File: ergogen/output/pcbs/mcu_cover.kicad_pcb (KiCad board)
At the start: 2 copper layers, 20.5 x 58 mm, 2 parts

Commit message: new shape
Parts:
- moved MH1 3.63 mm to (149.5, 86.4)
- moved MH2 2.39 mm to (163.5, 94.5)
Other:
- board size 20.5 x 58 mm -> 20.2 x 59 mm
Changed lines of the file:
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@@
   (title_block
     (title "mcu_cover")
-    (date "2025-11-02")
+    (date "2025-11-10")
     (rev "1")
     (company "curtis bollinger")
@@
   (footprint "ceoloide:mounting_hole_npth"
     (layer "F.Cu")
-    (at 151.2922031 89.53066630000001 0)
+    (at 149.48162050000002 86.38459739999999 0)
     (property "Reference" "MH1"
       (at 0 2.55 0)
@@
   (footprint "ceoloide:mounting_hole_npth"
     (layer "F.Cu")
-    (at 165.2922031 96.03066630000001 0)
+    (at 163.48162050000002 94.46459739999999 0)
     (property "Reference" "MH2"
       (at 0 2.55 0)
@@
     )
   )
-  (gr_line (start 168.7922031 100.07308144572157) (end 168.7922031 44.03066630000001) (layer Edge.Cuts) (stroke (width 0.15) (type default)))
-(gr_line (start 167.7922031 43.03066630000001) (end 149.2922031 43.03066630000001) (layer Edge.Cuts) (stroke (width 0.15) (type default)))
-(gr_line (start 148.2922031 90.64686063325334) (end 148.2922031 44.03066630000001) (layer Edge.Cuts) (stroke (width 0.15) (type default)))
-(gr_line (start 148.8382126 91.53786713325334) (end 167.33821260000002 100.96408794572159) (layer Edge.Cuts) (stroke (width 0.15) (type default)))
-(gr_line (start 153.1922031 76.93066630000001) (end 162.9922031 76.93066630000001) (layer Edge.Cuts) (stroke (width 0.15) (type default)))
-(gr_line (start 163.4922031 76.43066630000001) (end 163.4922031 52.130666300000016) (layer Edge.Cuts) (stroke (width 0.15) (type default)))
-(gr_line (start 162.9922031 51.630666300000016) (end 153.1922031 51.630666300000016) (layer Edge.Cuts) (stroke (width 0.15) (type default)))
-(gr_line (start 152.6922031 52.130666300000016) (end 152.6922031 76.43066630000001) (layer Edge.Cuts) (stroke (width 0.15) (type default)))
-(gr_arc (start 162.9922031 76.93066630000001) (mid 163.34575650000002 76.78421970000001) (end 163.4922031 76.43066630000001) (layer Edge.Cuts) (stroke (width 0.15) (type default)))
-(gr_arc (start 163.4922031 52.130666300000016) (mid 163.34575650000002 51.77711290000001) (end 162.9922031 51.630666300000016) (layer Edge.Cuts) (stroke (width 0.15) (type default)))
-(gr_arc (start 153.1922031 51.630666300000016) (mid 152.8386497 51.77711290000001) (end 152.6922031 52.130666300000016) (layer Edge.Cuts) (stroke (width 0.15) (type default)))
-(gr_arc (start 152.6922031 76.43066630000001) (mid 152.8386497 76.78421970000001) (end 153.1922031 76.93066630000001) (layer Edge.Cuts) (stroke (width 0.15) (type default)))
-(gr_arc (start 168.7922031 44.03066630000001) (mid 168.4993099 43.32355950000001) (end 167.7922031 43.03066630000001) (layer Edge.Cuts) (stroke (width 0.15) (type default)))
-(gr_arc (start 149.2922031 43.03066630000001) (mid 148.5850963 43.32355950000001) (end 148.2922031 44.03066630000001) (layer Edge.Cuts) (stroke (width 0.15) (type default)))
-(gr_arc (start 148.2922031 90.64686063325334) (mid 148.4395629 91.16935923325335) (end 148.8382126 91.53786713325334) (layer Edge.Cuts) (stroke (width 0.15) (type default)))
-(gr_arc (start 167.3382126 100.96408794572157) (mid 168.3147016 100.92572154572157) (end 168.7922031 100.07308144572157) (layer Edge.Cuts) (stroke (width 0.15) (type default)))
-(gr_circle (center 151.2922031 89.53066630000001) (end 152.2922031 89.53066630000001) (layer Edge.Cuts) (stroke (width 0.15) (type default)) (fill none))
-(gr_circle (center 165.2922031 96.03066630000001) (end 166.2922031 96.03066630000001) (layer Edge.Cuts) (stroke (width 0.15) (type default)) (fill none))
+  (gr_line (start 166.73162050017376 96.47131793428673) (end 166.73162050017376 41.4845974) (layer Edge.Cuts) (stroke (width 0.15) (type default)))
+(gr_line (start 164.73162050017376 39.4845974) (end 148.55712050000002 39.4845974) (layer Edge.Cuts) (stroke (width 0.15) (type default)))
+(gr_line (start 146.55712050000002 85.97848666737389) (end 146.55712050000002 41.4845974) (layer Edge.Cuts) (stroke (width 0.15) (type default)))
+(gr_line (start 148.55712050000005 89.44258826737392) (end 157.02419341559587 94.33105510345534) (layer Edge.Cuts) (stroke (width 0.15) (type default)))
+(gr_arc (start 146.55712050000002 85.97848666737389) (mid 147.09301890000003 87.97848666737389) (end 148.55712050000002 89.44258826737389) (layer Edge.Cuts) (stroke (width 0.15) (type default)))
+(gr_line (start 163.73162050017373 98.20336873428671) (end 157.0242892 94.33088919999997) (layer Edge.Cuts) (stroke (width 0.15) (type default)))
+(gr_line (start 157.0242892 94.33088919999997) (end 157.02419341559587 94.33105510345536) (layer Edge.Cuts) (stroke (width 0.15) (type default)))
+(gr_line (start 151.38162050000003 73.7845974) (end 161.18162050000004 73.7845974) (layer Edge.Cuts) (stroke (width 0.15) (type default)))
+(gr_line (start 161.68162050000004 73.2845974) (end 161.68162050000004 48.9845974) (layer Edge.Cuts) (stroke (width 0.15) (type default)))
+(gr_line (start 161.18162050000004 48.4845974) (end 151.38162050000003 48.4845974) (layer Edge.Cuts) (stroke (width 0.15) (type default)))
+(gr_line (start 150.88162050000003 48.9845974) (end 150.88162050000003 73.2845974) (layer Edge.Cuts) (stroke (width 0.15) (type default)))
+(gr_arc (start 161.18162050000004 73.7845974) (mid 161.53517390000005 73.63815079999999) (end 161.68162050000004 73.2845974) (layer Edge.Cuts) (stroke (width 0.15) (type default)))
+(gr_arc (start 161.68162050000004 48.9845974) (mid 161.53517390000005 48.631043999999996) (end 161.18162050000004 48.4845974) (layer Edge.Cuts) (stroke (width 0.15) (type default)))
+(gr_arc (start 151.38162050000003 48.4845974) (mid 151.02806710000002 48.631043999999996) (end 150.88162050000003 48.9845974) (layer Edge.Cuts) (stroke (width 0.15) (type default)))
+(gr_arc (start 150.88162050000003 73.2845974) (mid 151.02806710000002 73.63815079999999) (end 151.38162050000003 73.7845974) (layer Edge.Cuts) (stroke (width 0.15) (type default)))
+(gr_arc (start 166.73162050017376 41.4845974) (mid 166.14583410017377 40.0703838) (end 164.73162050017376 39.4845974) (layer Edge.Cuts) (stroke (width 0.15) (type default)))
+(gr_arc (start 148.55712050000002 39.4845974) (mid 147.1429069 40.0703838) (end 146.55712050000002 41.4845974) (layer Edge.Cuts) (stroke (width 0.15) (type default)))
+(gr_arc (start 163.73162050017376 98.20336873428673) (mid 165.73162050017376 98.20336873428673) (end 166.73162050017376 96.47131793428673) (layer Edge.Cuts) (stroke (width 0.15) (type default)))
+(gr_circle (center 149.48162050000002 86.38459739999999) (end 150.48162050000002 86.38459739999999) (layer Edge.Cuts) (stroke (width 0.15) (type default)) (fill none))
+(gr_circle (center 163.48162050000002 94.46459739999999) (end 164.48162050000002 94.46459739999999) (layer Edge.Cuts) (stroke (width 0.15) (type default)) (fill none))
 )

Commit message: update generated files
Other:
- board size 20.2 x 59 mm -> 20.2 x 59.7 mm
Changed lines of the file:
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@@
   (title_block
     (title "mcu_cover")
-    (date "2025-11-10")
+    (date "2025-11-12")
     (rev "1")
     (company "curtis bollinger")
@@
     )
   )
-  (gr_line (start 166.73162050017376 96.47131793428673) (end 166.73162050017376 41.4845974) (layer Edge.Cuts) (stroke (width 0.15) (type default)))
-(gr_line (start 164.73162050017376 39.4845974) (end 148.55712050000002 39.4845974) (layer Edge.Cuts) (stroke (width 0.15) (type default)))
-(gr_line (start 146.55712050000002 85.97848666737389) (end 146.55712050000002 41.4845974) (layer Edge.Cuts) (stroke (width 0.15) (type default)))
+  (gr_line (start 166.73162050017376 98.20336873864981) (end 166.73162050000002 43.4845974) (layer Edge.Cuts) (stroke (width 0.15) (type default)))
+(gr_line (start 147.55712050000002 39.4845974) (end 162.73162050000002 39.4845974) (layer Edge.Cuts) (stroke (width 0.15) (type default)))
+(gr_arc (start 166.73162050000002 43.4845974) (mid 165.56004760000002 40.6561703) (end 162.73162050000002 39.4845974) (layer Edge.Cuts) (stroke (width 0.15) (type default)))
+(gr_line (start 146.55712050000002 85.97848666737389) (end 146.55712050000002 40.4845974) (layer Edge.Cuts) (stroke (width 0.15) (type default)))
 (gr_line (start 148.55712050000005 89.44258826737392) (end 157.02419341559587 94.33105510345534) (layer Edge.Cuts) (stroke (width 0.15) (type default)))
 (gr_arc (start 146.55712050000002 85.97848666737389) (mid 147.09301890000003 87.97848666737389) (end 148.55712050000002 89.44258826737389) (layer Edge.Cuts) (stroke (width 0.15) (type default)))
-(gr_line (start 163.73162050017373 98.20336873428671) (end 157.0242892 94.33088919999997) (layer Edge.Cuts) (stroke (width 0.15) (type default)))
+(gr_line (start 165.23162050017376 99.06939413864981) (end 157.0242892 94.33088919999997) (layer Edge.Cuts) (stroke (width 0.15) (type default)))
 (gr_line (start 157.0242892 94.33088919999997) (end 157.02419341559587 94.33105510345536) (layer Edge.Cuts) (stroke (width 0.15) (type default)))
 (gr_line (start 151.38162050000003 73.7845974) (end 161.18162050000004 73.7845974) (layer Edge.Cuts) (stroke (width 0.15) (type default)))
@@
 (gr_arc (start 151.38162050000003 48.4845974) (mid 151.02806710000002 48.631043999999996) (end 150.88162050000003 48.9845974) (layer Edge.Cuts) (stroke (width 0.15) (type default)))
 (gr_arc (start 150.88162050000003 73.2845974) (mid 151.02806710000002 73.63815079999999) (end 151.38162050000003 73.7845974) (layer Edge.Cuts) (stroke (width 0.15) (type default)))
-(gr_arc (start 166.73162050017376 41.4845974) (mid 166.14583410017377 40.0703838) (end 164.73162050017376 39.4845974) (layer Edge.Cuts) (stroke (width 0.15) (type default)))
-(gr_arc (start 148.55712050000002 39.4845974) (mid 147.1429069 40.0703838) (end 146.55712050000002 41.4845974) (layer Edge.Cuts) (stroke (width 0.15) (type default)))
-(gr_arc (start 163.73162050017376 98.20336873428673) (mid 165.73162050017376 98.20336873428673) (end 166.73162050017376 96.47131793428673) (layer Edge.Cuts) (stroke (width 0.15) (type default)))
+(gr_arc (start 147.55712050000002 39.4845974) (mid 146.85001370000003 39.7774906) (end 146.55712050000002 40.4845974) (layer Edge.Cuts) (stroke (width 0.15) (type default)))
+(gr_arc (start 165.23162050017376 99.06939413864981) (mid 166.23162050017376 99.06939413864981) (end 166.73162050017376 98.20336873864981) (layer Edge.Cuts) (stroke (width 0.15) (type default)))
 (gr_circle (center 149.48162050000002 86.38459739999999) (end 150.48162050000002 86.38459739999999) (layer Edge.Cuts) (stroke (width 0.15) (type default)) (fill none))
 (gr_circle (center 163.48162050000002 94.46459739999999) (end 164.48162050000002 94.46459739999999) (layer Edge.Cuts) (stroke (width 0.15) (type default)) (fill none))

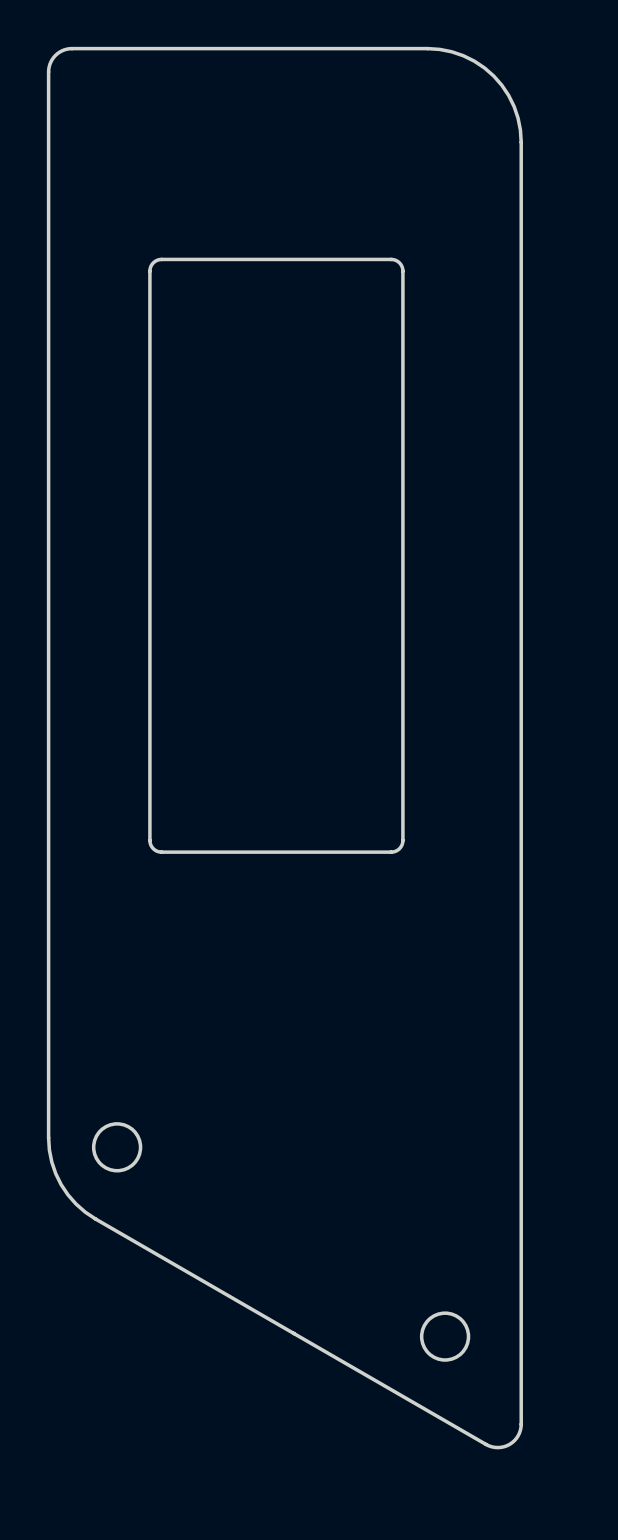
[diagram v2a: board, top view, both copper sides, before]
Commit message: working on new case
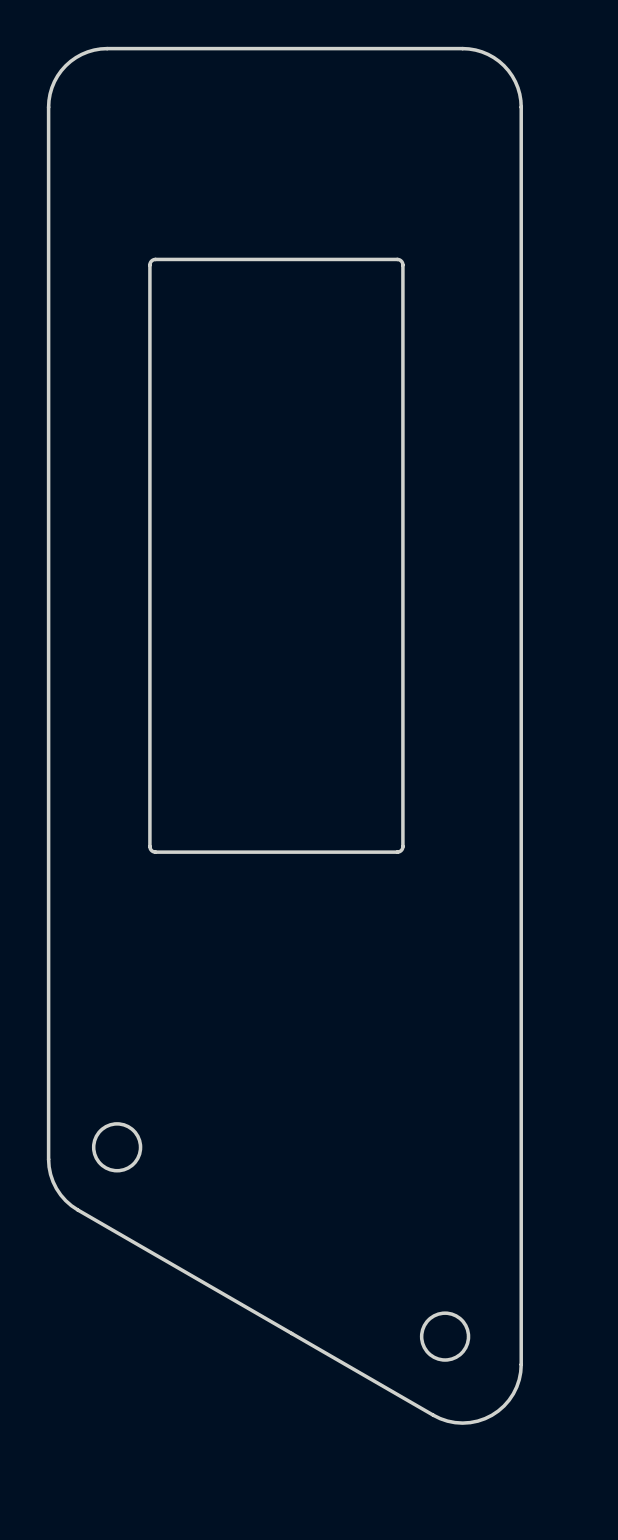
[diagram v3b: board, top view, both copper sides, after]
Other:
- board size 20.2 x 59.7 mm -> 20.2 x 58.7 mm
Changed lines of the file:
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@@
     )
   )
-  (gr_line (start 166.73162050017376 98.20336873864981) (end 166.73162050000002 43.4845974) (layer Edge.Cuts) (stroke (width 0.15) (type default)))
-(gr_line (start 147.55712050000002 39.4845974) (end 162.73162050000002 39.4845974) (layer Edge.Cuts) (stroke (width 0.15) (type default)))
-(gr_arc (start 166.73162050000002 43.4845974) (mid 165.56004760000002 40.6561703) (end 162.73162050000002 39.4845974) (layer Edge.Cuts) (stroke (width 0.15) (type default)))
-(gr_line (start 146.55712050000002 85.97848666737389) (end 146.55712050000002 40.4845974) (layer Edge.Cuts) (stroke (width 0.15) (type default)))
-(gr_line (start 148.55712050000005 89.44258826737392) (end 157.02419341559587 94.33105510345534) (layer Edge.Cuts) (stroke (width 0.15) (type default)))
-(gr_arc (start 146.55712050000002 85.97848666737389) (mid 147.09301890000003 87.97848666737389) (end 148.55712050000002 89.44258826737389) (layer Edge.Cuts) (stroke (width 0.15) (type default)))
-(gr_line (start 165.23162050017376 99.06939413864981) (end 157.0242892 94.33088919999997) (layer Edge.Cuts) (stroke (width 0.15) (type default)))
-(gr_line (start 157.0242892 94.33088919999997) (end 157.02419341559587 94.33105510345536) (layer Edge.Cuts) (stroke (width 0.15) (type default)))
-(gr_line (start 151.38162050000003 73.7845974) (end 161.18162050000004 73.7845974) (layer Edge.Cuts) (stroke (width 0.15) (type default)))
-(gr_line (start 161.68162050000004 73.2845974) (end 161.68162050000004 48.9845974) (layer Edge.Cuts) (stroke (width 0.15) (type default)))
-(gr_line (start 161.18162050000004 48.4845974) (end 151.38162050000003 48.4845974) (layer Edge.Cuts) (stroke (width 0.15) (type default)))
-(gr_line (start 150.88162050000003 48.9845974) (end 150.88162050000003 73.2845974) (layer Edge.Cuts) (stroke (width 0.15) (type default)))
-(gr_arc (start 161.18162050000004 73.7845974) (mid 161.53517390000005 73.63815079999999) (end 161.68162050000004 73.2845974) (layer Edge.Cuts) (stroke (width 0.15) (type default)))
-(gr_arc (start 161.68162050000004 48.9845974) (mid 161.53517390000005 48.631043999999996) (end 161.18162050000004 48.4845974) (layer Edge.Cuts) (stroke (width 0.15) (type default)))
-(gr_arc (start 151.38162050000003 48.4845974) (mid 151.02806710000002 48.631043999999996) (end 150.88162050000003 48.9845974) (layer Edge.Cuts) (stroke (width 0.15) (type default)))
-(gr_arc (start 150.88162050000003 73.2845974) (mid 151.02806710000002 73.63815079999999) (end 151.38162050000003 73.7845974) (layer Edge.Cuts) (stroke (width 0.15) (type default)))
-(gr_arc (start 147.55712050000002 39.4845974) (mid 146.85001370000003 39.7774906) (end 146.55712050000002 40.4845974) (layer Edge.Cuts) (stroke (width 0.15) (type default)))
-(gr_arc (start 165.23162050017376 99.06939413864981) (mid 166.23162050017376 99.06939413864981) (end 166.73162050017376 98.20336873864981) (layer Edge.Cuts) (stroke (width 0.15) (type default)))
+  (gr_line (start 166.7316204652048 95.6574636595821) (end 166.7316204652048 41.9845974) (layer Edge.Cuts) (stroke (width 0.15) (type default)))
+(gr_line (start 164.2316204652048 39.4845974) (end 149.05712050000002 39.4845974) (layer Edge.Cuts) (stroke (width 0.15) (type default)))
+(gr_line (start 146.55712050000002 86.89647358900609) (end 146.55712050000002 41.9845974) (layer Edge.Cuts) (stroke (width 0.15) (type default)))
+(gr_line (start 147.8071205 89.06153708900608) (end 156.9341933851923 94.33105508590181) (layer Edge.Cuts) (stroke (width 0.15) (type default)))
+(gr_arc (start 146.55712050000002 86.89647358900609) (mid 146.89205700000002 88.14647358900609) (end 147.80712050000002 89.0615370890061) (layer Edge.Cuts) (stroke (width 0.15) (type default)))
+(gr_line (start 162.98162046347275 97.82252715858212) (end 156.9341984 94.33104639999999) (layer Edge.Cuts) (stroke (width 0.15) (type default)))
+(gr_arc (start 166.7316204652048 41.9845974) (mid 165.9993874652048 40.2168304) (end 164.2316204652048 39.4845974) (layer Edge.Cuts) (stroke (width 0.15) (type default)))
+(gr_arc (start 149.05712050000002 39.4845974) (mid 147.28935350000003 40.2168304) (end 146.55712050000002 41.9845974) (layer Edge.Cuts) (stroke (width 0.15) (type default)))
+(gr_arc (start 162.9816204652048 97.82252715958211) (mid 165.4816204652048 97.82252715958211) (end 166.7316204652048 95.6574636595821) (layer Edge.Cuts) (stroke (width 0.15) (type default)))
+(gr_line (start 151.12162050000003 73.7845974) (end 161.44162050000003 73.7845974) (layer Edge.Cuts) (stroke (width 0.15) (type default)))
+(gr_line (start 161.68162050000004 73.5445974) (end 161.68162050000004 48.7245974) (layer Edge.Cuts) (stroke (width 0.15) (type default)))
+(gr_line (start 161.44162050000003 48.4845974) (end 151.12162050000003 48.4845974) (layer Edge.Cuts) (stroke (width 0.15) (type default)))
+(gr_line (start 150.88162050000003 48.7245974) (end 150.88162050000003 73.5445974) (layer Edge.Cuts) (stroke (width 0.15) (type default)))
+(gr_arc (start 162.9816204652048 97.82252715958211) (mid 162.9816204652048 97.82252715958211) (end 162.9816204652048 97.82252715958211) (layer Edge.Cuts) (stroke (width 0.15) (type default)))
+(gr_arc (start 161.44162050000003 73.7845974) (mid 161.6113261 73.714303) (end 161.68162050000004 73.5445974) (layer Edge.Cuts) (stroke (width 0.15) (type default)))
+(gr_arc (start 161.68162050000004 48.7245974) (mid 161.6113261 48.5548918) (end 161.44162050000003 48.4845974) (layer Edge.Cuts) (stroke (width 0.15) (type default)))
+(gr_arc (start 151.12162050000003 48.4845974) (mid 150.95191490000005 48.5548918) (end 150.88162050000003 48.7245974) (layer Edge.Cuts) (stroke (width 0.15) (type default)))
+(gr_arc (start 150.88162050000003 73.5445974) (mid 150.95191490000005 73.714303) (end 151.12162050000003 73.7845974) (layer Edge.Cuts) (stroke (width 0.15) (type default)))
 (gr_circle (center 149.48162050000002 86.38459739999999) (end 150.48162050000002 86.38459739999999) (layer Edge.Cuts) (stroke (width 0.15) (type default)) (fill none))
 (gr_circle (center 163.48162050000002 94.46459739999999) (end 164.48162050000002 94.46459739999999) (layer Edge.Cuts) (stroke (width 0.15) (type default)) (fill none))
